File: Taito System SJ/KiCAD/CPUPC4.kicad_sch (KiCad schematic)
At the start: 65 parts, among them U1 74LS138, U12 74LS10, U14 RAM_2016, U15 74LS367, U16 74LS367, U2 74LS138, U20 74LS138, U21 74LS04, U22 74LS86, U27 74LS367, U28 74LS367, U3 74LS32, U32 74LS367, U34 74LS08, U35 74LS32, U36 74LS04, U39 Z80-A (MAIN CPU), U40 74LS367, U41 74LS367, U45 74LS367, U50 74LS367, U52 M2732 - ROM10, U53 M2732 - ROM9, U54 M2732 - ROM8, U55 M2732 - ROM7, U61 74LS02, U62 74LS00, U64 M2732 - ROM6, U65 M2732 - ROM5, U66 M2732 - ROM4, U67 M2732 - ROM3, U68 M2732 - ROM2, U69 M2732 - ROM1, U7 74LS374, U76 74LS138, U77 74LS157, U78 74LS393, U79 74LS04, U8 74LS374, U84 74LS32, U85 74LS74, U86 74LS04, U87 74LS74, U88 74LS04, U89 74LS74, U9 74LS173, U90 74LS74, U91 74LS25, U92 74LS74, U96 74LS08, U98 74LS00

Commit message: Start of gameboard
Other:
- company: (none) -> ANTON GALE
- title: (none) -> TAITO SYSTEM SJ
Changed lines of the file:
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@@
 (kicad_sch (version 20211123) (generator eeschema)
   (paper "D")
+  (title_block
+    (title "TAITO SYSTEM SJ")
+    (company "ANTON GALE")
+  )
   (junction (at 637.54 210.82) (diameter 0) (color 0 0 0 0)
   )

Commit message: Update before transfer
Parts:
- U32: value 74LS367 -> 74LS96
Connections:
- net CD0: no longer U32.13 (O6b)
- net CD1: no longer U32.11 (O5b)
- net D0: no longer U32.14 (I6)
- net D1: now also U32.9 (SER); no longer U32.12 (I5)
- net VCC: now also U32.5 (VCC)
- net ~{WRA}: no longer U32.15 (OEb)
- new net GND: U32.12 (GND)

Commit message: Component naming updates
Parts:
- added U111: 74LS04, symbol 74xx:74LS04
- gave numbers to parts that had none: 1
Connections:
- net A15: now also U111.13
- net ~{CPUMREQ}: now also U76.5 (E2)
- net ~{RD}: now also U76.4 (E1)
- net ~{READ}: now also U2.11 (O4)
- net ~{SMD12}: no longer U2.11 (O4)
- net ~{SMD3}: no longer U2.10 (O5), U20.4 (E1)
- net at U76.6 (E3): now also U111.12
- net BANKSEL renamed BANK_SEL
- new net ~{WRITE}: U2.10 (O5), U20.4 (E1)
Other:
- moved on the sheet: U76, U77

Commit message: Multiple updates while coding core
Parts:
- removed U32: 74LS96, symbol jt74:74LS367
- removed U45: 74LS367, symbol jt74:74LS367
- removed U7: 74LS374, symbol jt74:74LS374
- added U55: 74LS138, symbol jt74:74LS138
- gave numbers to parts that had none: 3
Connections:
- net A0: now also U55.1 (A0)
- net A1: now also U55.2 (A1)
- net A2: now also U55.3 (A2)
- net A3: now also U55.6 (E3)
- net ~{TIMERESET}: now also U55.10 (O5)
- net ~{WRITE}: now also U55.5 (E2)
- net ~{WR}: now also U55.4 (E1)
- net ~{1V'} renamed 1V'
- net ~{2V'} renamed 2V'
- net ~{4V'} renamed 4V'
- net ~{S.OFF} renamed ~{SOFF}
- new net ~{COIN_SET}: U55.9 (O6)
- new net ~{EPORT1}: U55.12 (O3)
- new net ~{EPORT2}: U55.11 (O4)
- new net ~{EXPORT}: U55.7 (O7)
- new net ~{EXROM1}: U55.14 (O1)
- new net ~{EXROM2}: U55.13 (O2)
- new net ~{HTCLR}: U55.15 (O0)
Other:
- note added: "THIS IS A DIFFERENT CDRRQ THAN THE ONE ON THE VIDEO BOARD"
- note added: "These signals are not going onto the bus, they are to send the signals to other boards"
- moved on the sheet: U1, U2, U20, U21C, U3A, U3B, U3C, U3D

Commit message: Tidied up loose ends
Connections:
- net C.INV renamed CINV
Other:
- note added: "9000-9FFF"
- note added: "A000-BFFF"
- note added: "C000-CFFF"
- note added: "D000-D0FF"
- note added: "D100-D1FF"
- note added: "D200-D2FF"
- note added: "D300-D3FF"
- note added: "D400-D4FF"
- note added: "D500"
- note added: "D500-D5FF"
- note added: "D501"
- note added: "D502"
- note added: "D503"
- note added: "D504"
- note added: "D505"
- note added: "D506"
- note added: "D507"
- note added: "D508"
- note added: "D509"
- note added: "D50A"
- note added: "D50B"
- note added: "D50C"
- note added: "D50D"
- note added: "D50E"
- note added: "D50F"
- note added: "D600-D6FF"
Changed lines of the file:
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@@
     (stroke (width 0) (type default))
+  )
+  (text "D504" (at 350.52 447.04 0)
+    (effects (font (size 1.27 1.27)) (justify left bottom))
+  )
+  (text "A000-BFFF" (at 350.52 335.28 0)
+    (effects (font (size 1.27 1.27)) (justify left bottom))
   )
   (text "THIS IS A DIFFERENT CDRRQ THAN \nTHE ONE ON THE VIDEO BOARD"
@@
     (effects (font (size 1.27 1.27)) (justify left bottom))
   )
+  (text "D50F" (at 350.52 487.68 0)
+    (effects (font (size 1.27 1.27)) (justify left bottom))
+  )
+  (text "D506" (at 350.52 441.96 0)
+    (effects (font (size 1.27 1.27)) (justify left bottom))
+  )
+  (text "D502" (at 350.52 452.12 0)
+    (effects (font (size 1.27 1.27)) (justify left bottom))
+  )
+  (text "D500" (at 350.52 457.2 0)
+    (effects (font (size 1.27 1.27)) (justify left bottom))
+  )
+  (text "D200-D2FF" (at 350.52 398.78 0)
+    (effects (font (size 1.27 1.27)) (justify left bottom))
+  )
+  (text "D509" (at 350.52 502.92 0)
+    (effects (font (size 1.27 1.27)) (justify left bottom))
+  )
+  (text "D503" (at 350.52 449.58 0)
+    (effects (font (size 1.27 1.27)) (justify left bottom))
+  )
+  (text "D508" (at 350.52 505.46 0)
+    (effects (font (size 1.27 1.27)) (justify left bottom))
+  )
+  (text "D300-D3FF" (at 350.52 378.46 0)
+    (effects (font (size 1.27 1.27)) (justify left bottom))
+  )
+  (text "D50E" (at 350.52 490.22 0)
+    (effects (font (size 1.27 1.27)) (justify left bottom))
+  )
+  (text "C000-CFFF" (at 350.52 313.69 0)
+    (effects (font (size 1.27 1.27)) (justify left bottom))
+  )
+  (text "D600-D6FF" (at 350.52 363.22 0)
+    (effects (font (size 1.27 1.27)) (justify left bottom))
+  )
+  (text "D50C" (at 350.52 495.3 0)
+    (effects (font (size 1.27 1.27)) (justify left bottom))
+  )
+  (text "D50D" (at 350.52 492.76 0)
+    (effects (font (size 1.27 1.27)) (justify left bottom))
+  )
+  (text "D500-D5FF" (at 350.52 391.16 0)
+    (effects (font (size 1.27 1.27)) (justify left bottom))
+  )
+  (text "D501" (at 350.52 454.66 0)
+    (effects (font (size 1.27 1.27)) (justify left bottom))
+  )
+  (text "D100-D1FF" (at 350.52 401.32 0)
+    (effects (font (size 1.27 1.27)) (justify left bottom))
+  )
   (text "*BANKSEL COMES FROM 'GAME BOARD'" (at 718.82 190.5 0)
+    (effects (font (size 1.27 1.27)) (justify left bottom))
+  )
+  (text "9000-9FFF" (at 350.52 340.36 0)
+    (effects (font (size 1.27 1.27)) (justify left bottom))
+  )
+  (text "D400-D4FF" (at 350.52 393.7 0)
+    (effects (font (size 1.27 1.27)) (justify left bottom))
+  )
+  (text "D000-D0FF" (at 350.52 403.86 0)
+    (effects (font (size 1.27 1.27)) (justify left bottom))
+  )
+  (text "D507" (at 350.52 439.42 0)
+    (effects (font (size 1.27 1.27)) (justify left bottom))
+  )
+  (text "D505" (at 350.52 444.5 0)
     (effects (font (size 1.27 1.27)) (justify left bottom))
   )
@@
     (effects (font (size 1.27 1.27)) (justify left bottom))
   )
+  (text "D50B" (at 350.52 497.84 0)
+    (effects (font (size 1.27 1.27)) (justify left bottom))
+  )
+  (text "D50A" (at 350.52 500.38 0)
+    (effects (font (size 1.27 1.27)) (justify left bottom))
+  )
   (label "Z80M_D1" (at 640.08 415.29 180) (fields_autoplaced)
     (effects (font (size 1.27 1.27)) (justify right bottom))
@@
     (effects (font (size 1.27 1.27)) (justify left bottom))
   )
-  (global_label "C.INV" (shape output) (at 162.56 379.73 0) (fields_autoplaced)
+  (global_label "CINV" (shape output) (at 162.56 379.73 0) (fields_autoplaced)
     (effects (font (size 1.27 1.27)) (justify left))
-    (property "Intersheetrefs" "${INTERSHEET_REFS}" (at 169.8717 379.6506 0)
+    (property "Intersheetrefs" "${INTERSHEET_REFS}" (at 169.7597 379.73 0)
       (effects (font (size 1.27 1.27)) (justify left) hide)
     )

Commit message: Added MCU to Taito SJ Schematics
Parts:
- added U?: 74LS04, symbol jt74:74LS04
- added U?: 74LS27, symbol jt74:74LS27
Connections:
- net A11: now also U?.1
- net A12: now also U?.2
- net ~{CDR1-2}: now also U?.13
- net ~{CPUWAIT}: now reaches U39.24 (~{WAIT}), U91.6 (Y)
- new net: U?.12, U?.5
- new net ~{SCRAM}: U?.6
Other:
- note added: "9000-9FFF - Character Generator RAM"
- note added: "A000-BFFF - Character Generator RAM"
- note added: "C000-CFFF - Tilemap RAM"
- note added: "D000-D0FF - Tilemap Column Scroll"
- note added: "D100-D1FF - Sprite position/attribute RAM"
- note added: "D200-D2FF - Palette RAM"
- note added: "D500 - Tilemap #1 Horizontal Scroll"
- note added: "D501 - Tilemap #1 Vertical Scroll"
- note added: "D502 - Tilemap #2 Horizontal Scroll"
- note added: "D503 - Tilemap #2 Vertical Scroll"
- note added: "D504 - Tilemap #3 Horizontal Scroll"
- note added: "D505 - Tilemap #3 Vertical Scroll"
- note added: "D506 - Tilemap #1 & #2 Color & Char Code"
- note added: "D507 - Tilemap #3 Color, Char Code & Sprite Colour Bank"
- note added: "D509 - Graphics ROM LO"
- note added: "D50A - Graphics ROM HI"
- note added: "D50B - Sound CPU Command"
- note added: "D50C - Sound CPU Command"
- note added: "D50D - Watchdog Reset"
- note added: "D50E - Coin Lockout"
- note added: "D800-DFFF - Scroll RAM"
- note removed: "9000-9FFF"
- note removed: "A000-BFFF"
- note removed: "C000-CFFF"
- note removed: "D000-D0FF"
- note removed: "D100-D1FF"
- note removed: "D200-D2FF"
- note removed: "D500"
- note removed: "D501"
- note removed: "D502"
- note removed: "D503"
- note removed: "D504"
- note removed: "D505"
- note removed: "D506"
- note removed: "D507"
- note removed: "D509"
- note removed: "D50A"
- note removed: "D50B"
- note removed: "D50C"
- note removed: "D50D"
- note removed: "D50E"

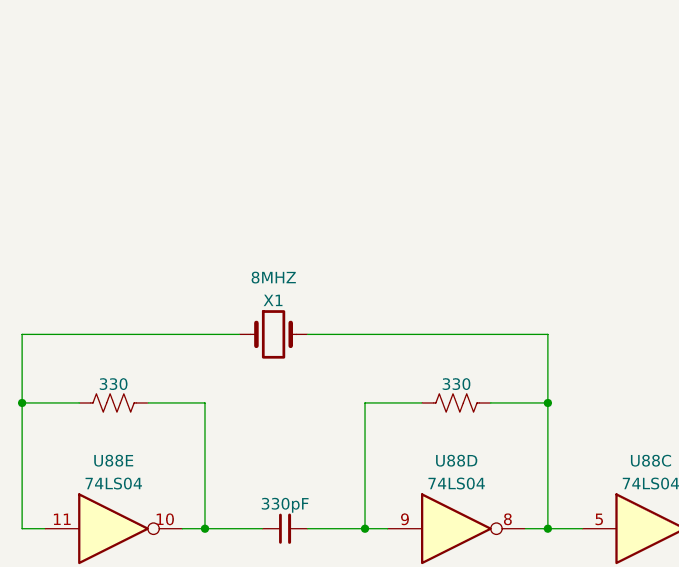
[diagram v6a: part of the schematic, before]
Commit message: Updated Taito SJ Schematics
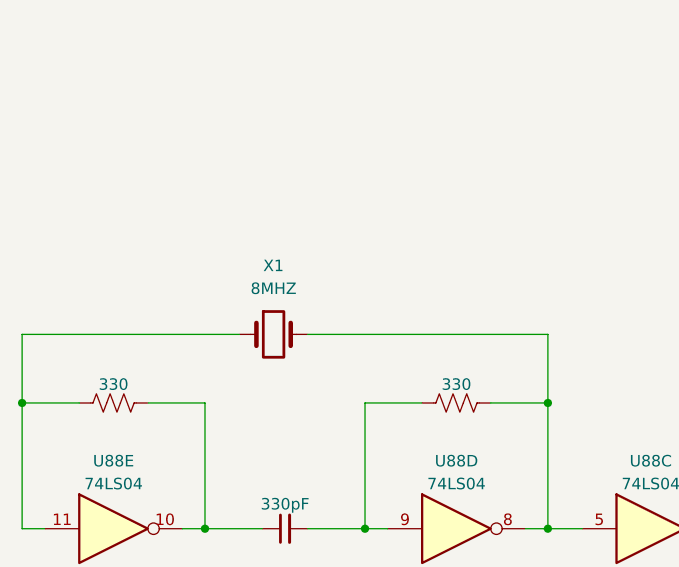
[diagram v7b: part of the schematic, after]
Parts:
- X1: renamed from 8MHZ; value X1 -> 8MHZ
